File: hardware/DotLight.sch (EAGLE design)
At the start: 21 parts, among them Q1 BSH103, Q2 BSH103

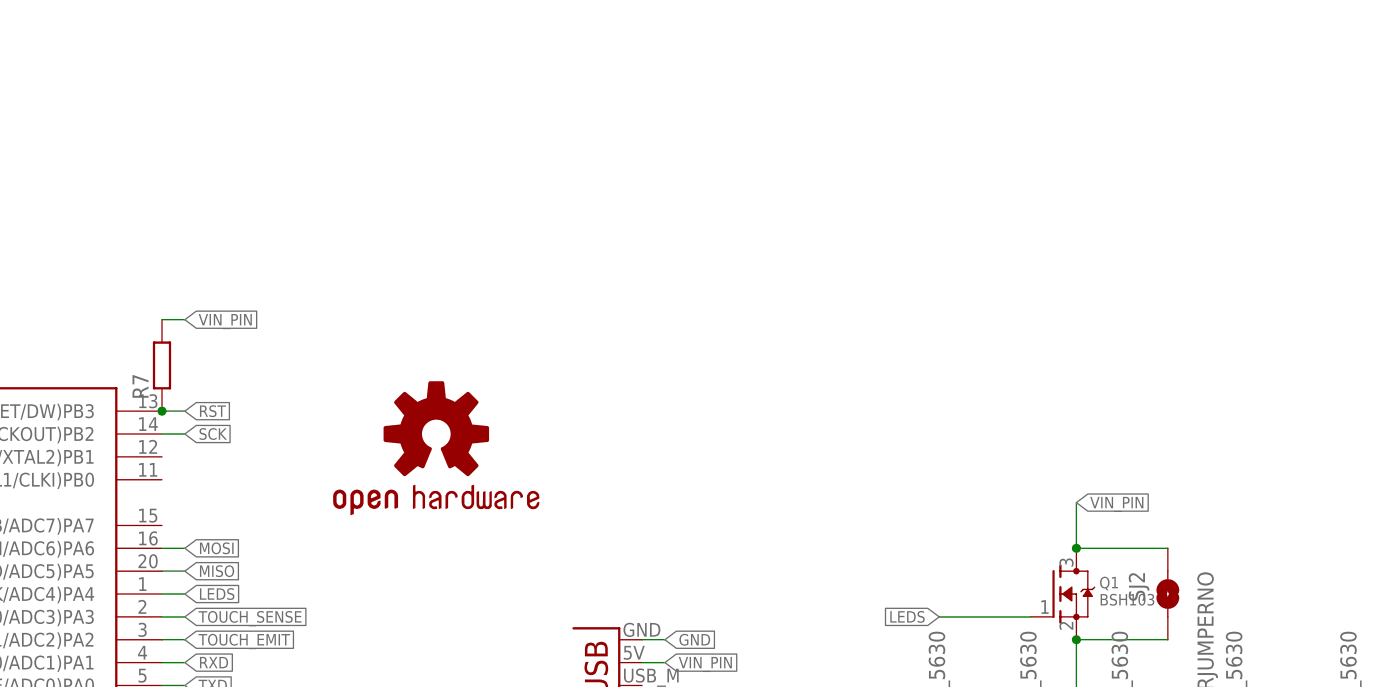
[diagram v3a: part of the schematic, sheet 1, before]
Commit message: Add RGB led
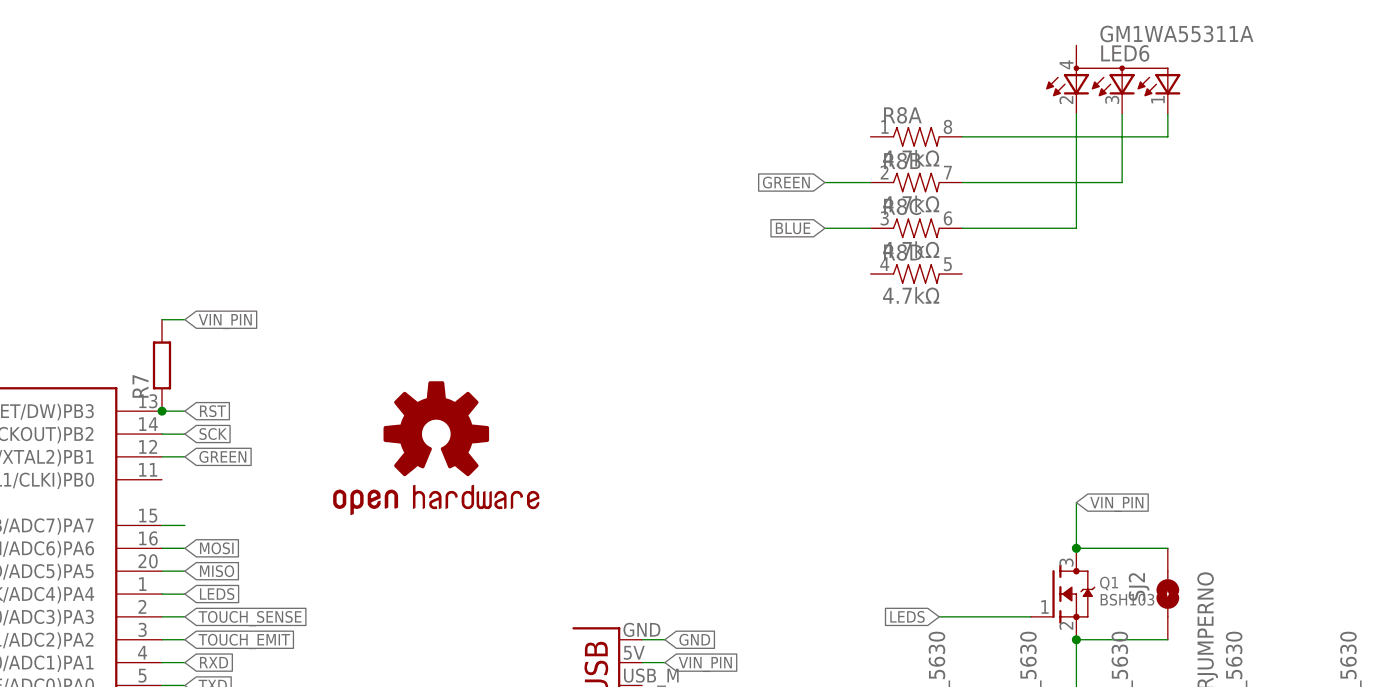
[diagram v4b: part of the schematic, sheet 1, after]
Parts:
- added LED6: GM1WA55311A, led:GM1WA55311A
- added R8: 4.7kΩ, SparkFun:RESISTOR-ARRAY0603-ARV
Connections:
- new net BLUE: R8C.1, U$1.(PCINT7/ICP/OC0B/ADC7)PA7
- new net GREEN: R8B.1, U$1.(PCINT9/XTAL2)PB1
- new net N$1: LED6.CRED, R8C.2
- new net N$2: LED6.CBLUE, R8B.2
- new net N$4: LED6.CGREEN, R8A.2
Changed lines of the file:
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@@
 <part name="SUPPLY2" library="supply2" deviceset="GND" device=""/>
 <part name="R7" library="rcl" deviceset="R-EU_" device="R0603"/>
+<part name="LED6" library="led" deviceset="GM1WA55311A" device=""/>
+<part name="R8" library="SparkFun" deviceset="RESISTOR-ARRAY" device="0603-ARV" value="4.7kΩ"/>
 </parts>
 <sheets>
@@
 <instance part="SUPPLY2" gate="GND" x="30.48" y="187.96"/>
 <instance part="R7" gate="G$1" x="81.28" y="226.06" rot="R90"/>
+<instance part="LED6" gate="G$1" x="187.96" y="259.08"/>
+<instance part="R8" gate="A" x="165.1" y="251.46"/>
+<instance part="R8" gate="B" x="165.1" y="246.38"/>
+<instance part="R8" gate="C" x="165.1" y="241.3"/>
+<instance part="R8" gate="D" x="165.1" y="236.22"/>
 </instances>
 <busses>
@@
 </segment>
 </net>
+<net name="N$1" class="0">
+<segment>
+<pinref part="R8" gate="C" pin="2"/>
+<pinref part="LED6" gate="G$1" pin="CRED"/>
+<wire x1="170.18" y1="241.3" x2="182.88" y2="241.3" width="0.1524" layer="91"/>
+<wire x1="182.88" y1="241.3" x2="182.88" y2="254" width="0.1524" layer="91"/>
+</segment>
+</net>
+<net name="N$2" class="0">
+<segment>
+<pinref part="LED6" gate="G$1" pin="CBLUE"/>
+<wire x1="187.96" y1="254" x2="187.96" y2="246.38" width="0.1524" layer="91"/>
+<pinref part="R8" gate="B" pin="2"/>
+<wire x1="187.96" y1="246.38" x2="170.18" y2="246.38" width="0.1524" layer="91"/>
+</segment>
+</net>
+<net name="N$4" class="0">
+<segment>
+<pinref part="R8" gate="A" pin="2"/>
+<pinref part="LED6" gate="G$1" pin="CGREEN"/>
+<wire x1="170.18" y1="251.46" x2="193.04" y2="251.46" width="0.1524" layer="91"/>
+<wire x1="193.04" y1="251.46" x2="193.04" y2="254" width="0.1524" layer="91"/>
+</segment>
+</net>
+<net name="BLUE" class="0">
+<segment>
+<pinref part="R8" gate="C" pin="1"/>
+<wire x1="160.02" y1="241.3" x2="154.94" y2="241.3" width="0.1524" layer="91"/>
+<label x="154.94" y="241.3" size="1.27" layer="95" rot="R180" xref="yes"/>
+</segment>
+<segment>
+<pinref part="U$1" gate="G$1" pin="(PCINT7/ICP/OC0B/ADC7)PA7"/>
+<wire x1="81.28" y1="208.28" x2="83.82" y2="208.28" width="0.1524" layer="91"/>
+</segment>
+</net>
+<net name="GREEN" class="0">
+<segment>
+<pinref part="R8" gate="B" pin="1"/>
+<wire x1="160.02" y1="246.38" x2="154.94" y2="246.38" width="0.1524" layer="91"/>
+<label x="154.94" y="246.38" size="1.27" layer="95" rot="R180" xref="yes"/>
+</segment>
+<segment>
+<pinref part="U$1" gate="G$1" pin="(PCINT9/XTAL2)PB1"/>
+<wire x1="81.28" y1="215.9" x2="83.82" y2="215.9" width="0.1524" layer="91"/>
+<label x="83.82" y="215.9" size="1.27" layer="95" xref="yes"/>
+</segment>
+</net>

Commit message: Add R to RGB
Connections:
- new net RED: R8A.1, U$1.(PCINT8/XTAL1/CLKI)PB0
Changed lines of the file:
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@@
 <pinref part="U$1" gate="G$1" pin="(PCINT7/ICP/OC0B/ADC7)PA7"/>
 <wire x1="81.28" y1="208.28" x2="83.82" y2="208.28" width="0.1524" layer="91"/>
+<label x="83.82" y="208.28" size="1.27" layer="95" xref="yes"/>
 </segment>
 </net>
@@
 </segment>
 </net>
+<net name="RED" class="0">
+<segment>
+<pinref part="U$1" gate="G$1" pin="(PCINT8/XTAL1/CLKI)PB0"/>
+<wire x1="81.28" y1="213.36" x2="83.82" y2="213.36" width="0.1524" layer="91"/>
+<label x="83.82" y="213.36" size="1.27" layer="95" xref="yes"/>
+</segment>
+<segment>
+<pinref part="R8" gate="A" pin="1"/>
+<wire x1="160.02" y1="251.46" x2="154.94" y2="251.46" width="0.1524" layer="91"/>
+<label x="154.94" y="251.46" size="1.27" layer="95" rot="R180" xref="yes"/>
+</segment>
+</net>

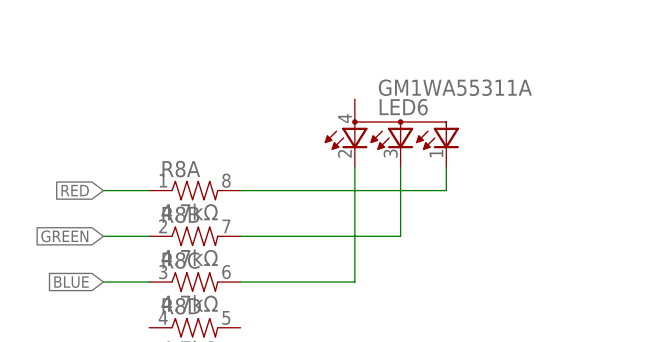
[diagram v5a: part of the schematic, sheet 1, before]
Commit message: Correct RGB 3V3
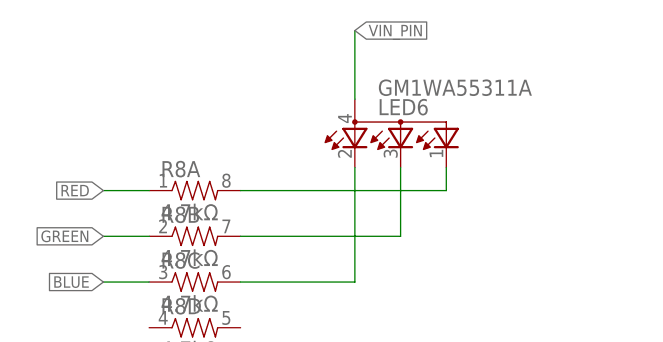
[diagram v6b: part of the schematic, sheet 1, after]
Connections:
- net VIN_PIN: now also LED6.A
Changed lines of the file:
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@@
 <label x="83.82" y="231.14" size="1.27" layer="95" xref="yes"/>
+</segment>
+<segment>
+<pinref part="LED6" gate="G$1" pin="A"/>
+<wire x1="182.88" y1="261.62" x2="182.88" y2="269.24" width="0.1524" layer="91"/>
+<label x="182.88" y="269.24" size="1.27" layer="95" xref="yes"/>
 </segment>
 </net>

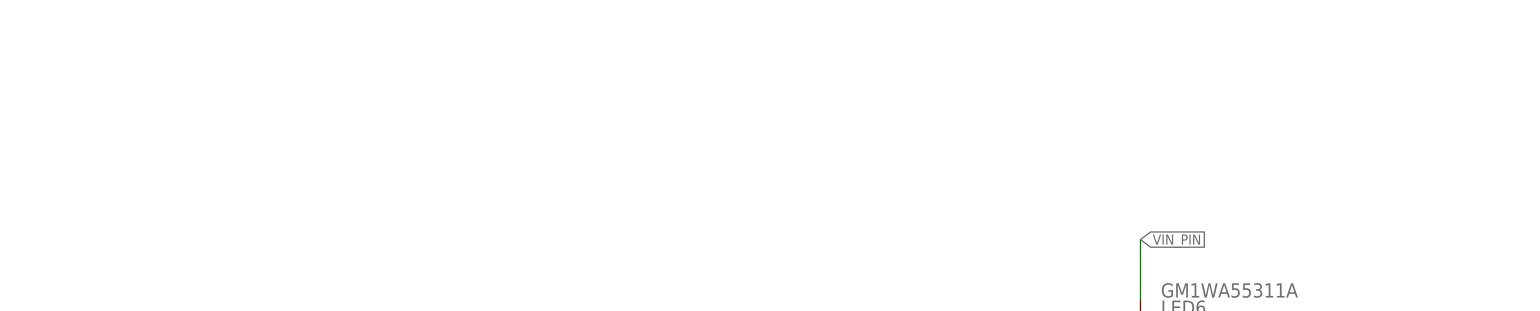
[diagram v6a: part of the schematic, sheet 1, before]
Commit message: Insert warning : using t84 instad of t85
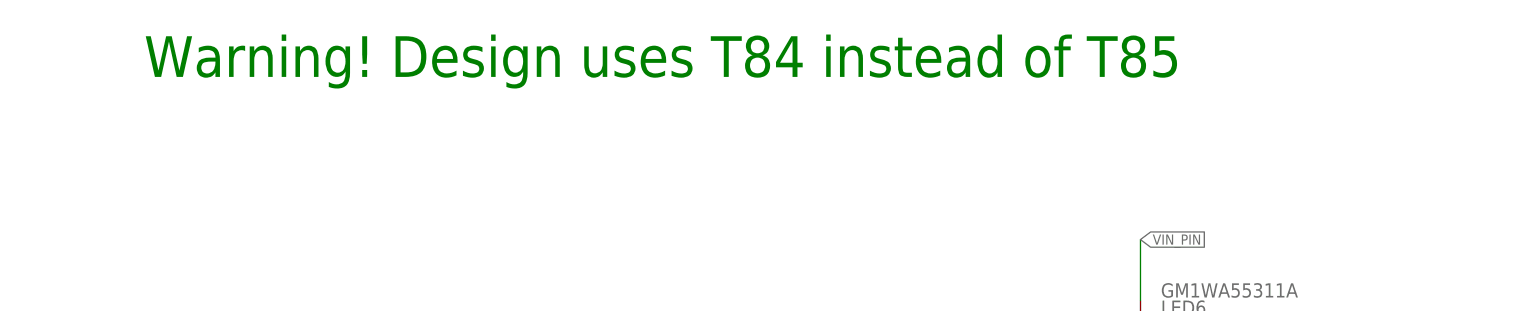
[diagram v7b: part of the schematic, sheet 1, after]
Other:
- note added: "Warning! Design uses T84 instead of T85"
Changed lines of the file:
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@@
 <text x="114.3" y="124.46" size="1.27" layer="91">Emit</text>
 <text x="139.7" y="124.46" size="1.27" layer="91">Sense</text>
+<text x="58.42" y="289.56" size="5.08" layer="91">Warning! Design uses T84 instead of T85</text>
 </plain>
 <instances>
